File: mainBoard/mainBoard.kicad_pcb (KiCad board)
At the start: 4 copper layers, 118.4 x 54.5 mm, 77 parts, among them J1 Conn_01x01, J10 Conn_01x05, J11 Conn_01x04, J12 Conn_01x01, J13 Conn_01x01, J14 Conn_01x01, J15 Conn_01x01, J16 Conn_01x01, J17 Conn_01x01, J18 Conn_01x01, J19 Conn_01x01, J2 Conn_01x01, J20 Conn_01x01, J21 Conn_01x01, J22 Conn_01x01, J23 Conn_01x05, J24 Conn_01x04, J25 Conn_01x05, J26 Conn_01x05, J27 Conn_01x05, J28 Conn_01x04, J29 Conn_01x04, J3 Conn_01x01, J30 Conn_01x04, J31 Conn_02x05_Odd_Even, J32 Conn_02x07_Odd_Even, J33 Conn_01x04, J34 Conn_01x02, J35 Conn_01x02, J36 Conn_01x03, J37 Conn_01x02, J38 Conn_01x02, J4 Conn_01x01, J5 Conn_01x01, J6 Conn_01x01, J7 Conn_01x01, J8 Conn_01x01, J9 Conn_01x01, M1 Conn_01x01, M2 Conn_01x01, U1 STM32H503CBT6, U2 DRV8251ADDAR, U3 MAX15062A, U4 64Kbit

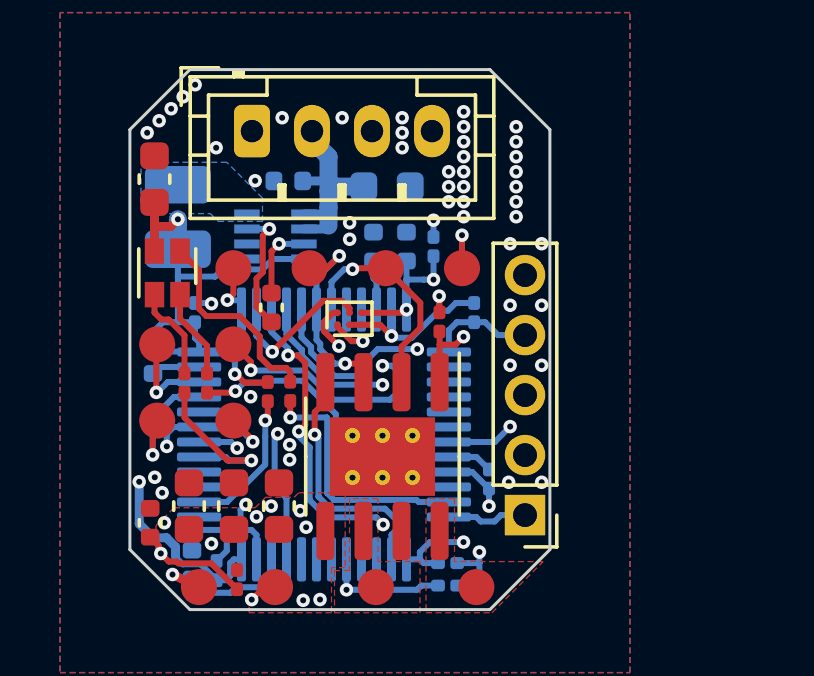
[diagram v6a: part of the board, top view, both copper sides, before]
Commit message: Expose boot0 so any user can shortcut to VCC
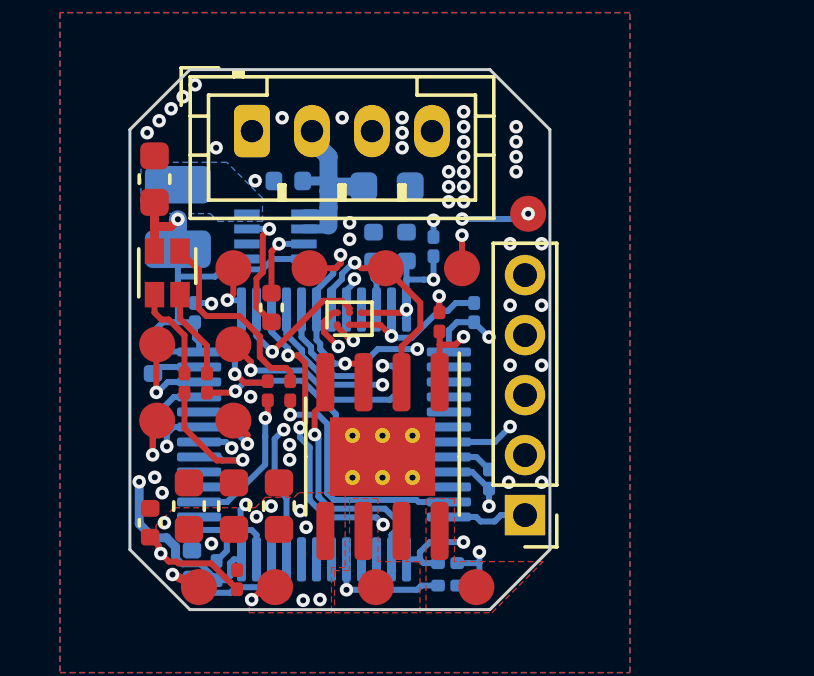
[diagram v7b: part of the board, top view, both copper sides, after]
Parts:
- added J39: Conn_01x01, RKL-Connectors:YZ157015035P-01-contact_pad, F.Cu at (106.9, 69.4)
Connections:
- J10 pad 4: VDD -> VSS
- J10 pad 5: VSS -> VDD
- U1 pad 44: unconnected-(U1-BOOT0-Pad44) -> /MotorBoard/CPU/BOOT
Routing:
- net /MotorBoard/CPU/BOOT: track 0.00 -> 7.82 mm, vias 0 -> 3
- net /MotorBoard/CPU/EEPROM.SDA: track 12.4 -> 10.3 mm
- net VDD: track 75.3 -> 73.9 mm, vias 6 -> 7
- net VSS: vias 53 -> 49

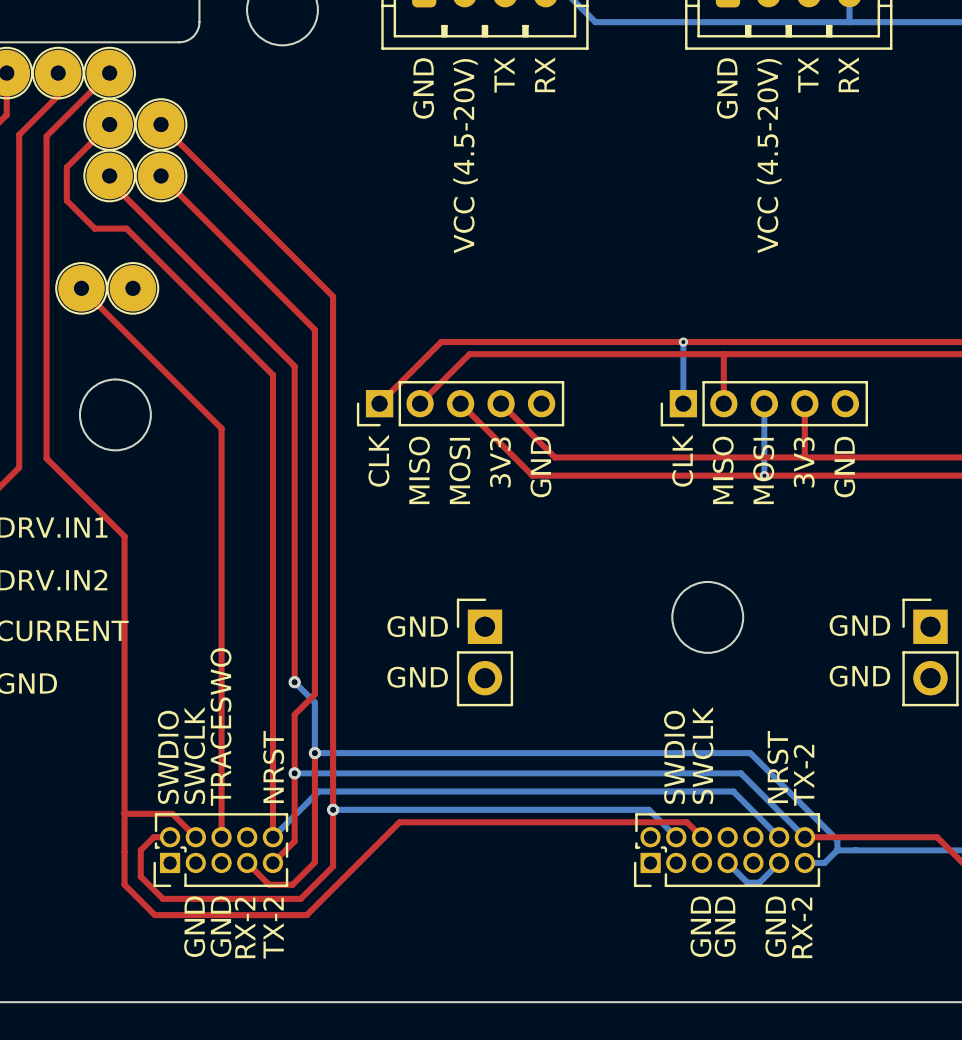
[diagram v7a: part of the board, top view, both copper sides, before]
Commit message: On debug board, For BMDU connector (J31) - make TX/RX wiring optional
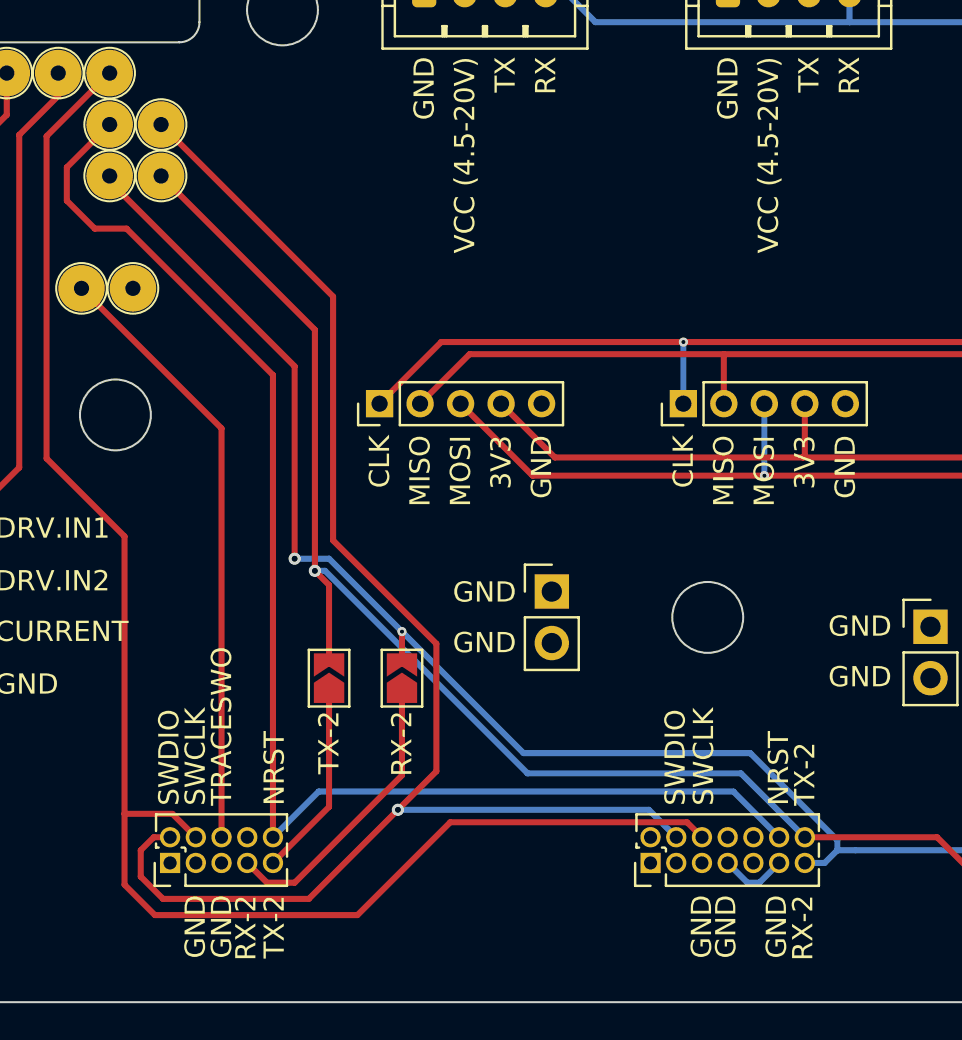
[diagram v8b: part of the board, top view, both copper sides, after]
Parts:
- added JP1: Jumper_2_Bridged, Jumper:SolderJumper-2_P1.3mm_Open_TrianglePad1.0x1.5mm, F.Cu at (150.3, 90.0)
- added JP2: Jumper_2_Bridged, Jumper:SolderJumper-2_P1.3mm_Open_TrianglePad1.0x1.5mm, F.Cu at (153.9, 90.0)
- moved J34 3.73 mm to (161.3, 85.7)
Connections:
- J31 pad 7: /DebuBoard/DB-TUNING-LINES.RX-2 -> Net-(J31-Pin_7)
- J31 pad 9: /DebuBoard/DB-TUNING-LINES.TX-2 -> Net-(J31-Pin_9)
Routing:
- net Net-(J31-Pin_7): track 0.00 -> 14.3 mm
- net /DebuBoard/DB-TUNING-LINES.RX-2: track 84.1 -> 71.0 mm
- net Net-(J31-Pin_9): track 0.00 -> 9.55 mm
- net /DebuBoard/DB-TUNING-LINES.TX-2: track 82.3 -> 75.0 mm
- net /DebuBoard/DB-TUNING-LINES.SWDIO: track 71.3 -> 72.6 mm
